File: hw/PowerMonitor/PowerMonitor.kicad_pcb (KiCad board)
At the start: 4 copper layers, 100 x 100 mm, 161 parts, among them J1 Conn_01x02_Socket, J2 Conn_01x02_Socket, J3 Conn_01x02_Socket, J4 Conn_01x02_Socket, J5 Conn_01x02_Socket, K1 Relay_SPST-NO, Q1 AO3400A, Q10 Q_PMOS_GDS, Q11 AO3400A, Q12 AO3400A, Q13 X0202MN, Q14 AO3400A, Q15 AO3400A, Q16 AO3400A, Q17 AO3400A, Q18 AO3400A, Q19 AO3400A, Q2 AO3400A, Q20 AO3400A, Q3 AO3400A, Q4 Q_PMOS_GDS, Q5 AO3400A, Q6 AO3400A, Q7 Q_PMOS_GDS, Q8 AO3400A, Q9 AO3400A, SW1 SW_Wuerth_450301014042, U1 LM393, U2 INA129, U3 LM358, U4 LM393, U5 LM358, U6 LM393, U7 LM358, U8 LM393

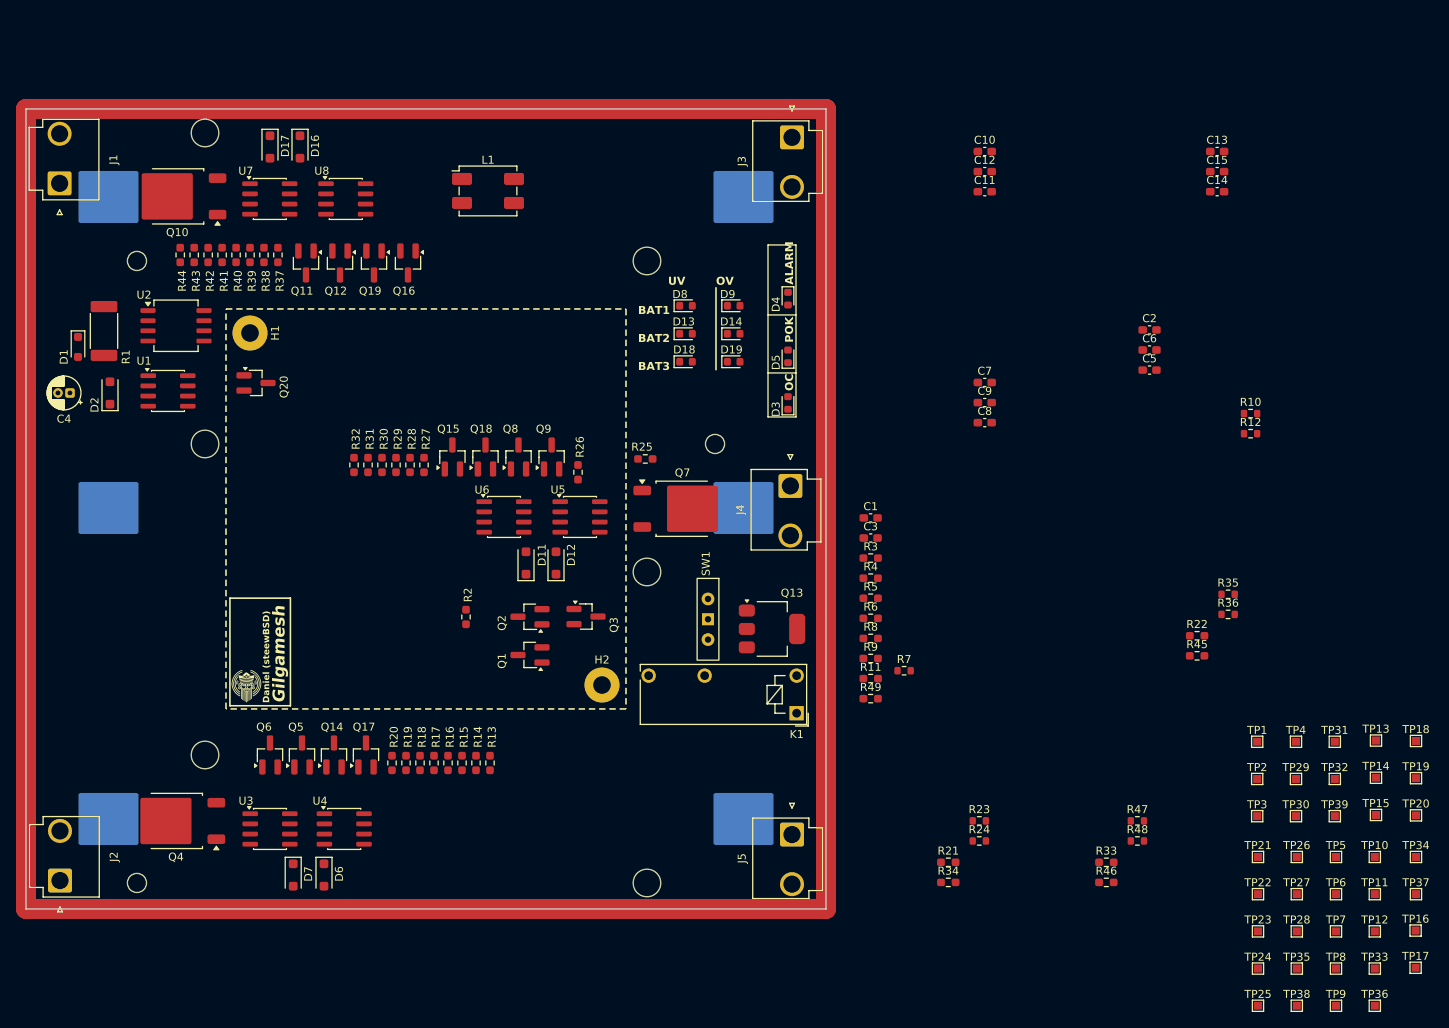
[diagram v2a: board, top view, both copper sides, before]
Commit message: finish PowerMonitor placement
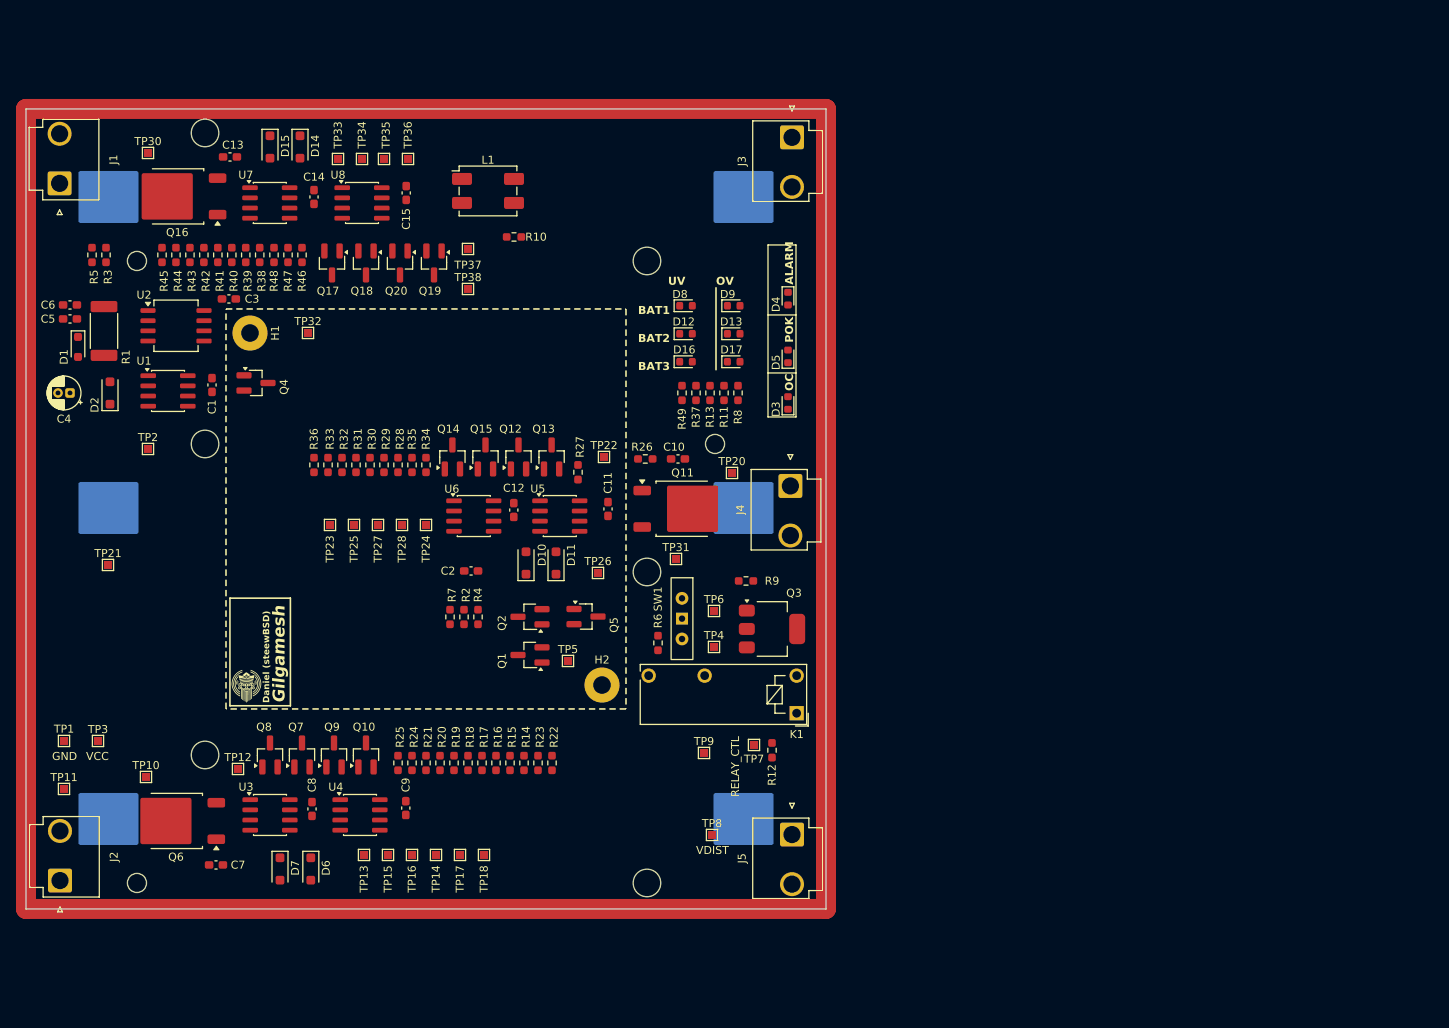
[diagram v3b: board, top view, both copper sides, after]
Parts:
- removed the R23 at (214.9, 129.5)
- removed the R35 at (246.0, 101.2)
- removed the R47 at (234.7, 129.5)
- removed the TP12 at (264.4, 143.3)
- removed the TP20 at (269.5, 128.8)
- removed the TP28 at (254.6, 143.3)
- added R24: 1K, Resistor_SMD:R_0603_1608Metric_Pad0.98x0.95mm_HandSolder, F.Cu at (144.0, 122.2)
- added R36: 1K, Resistor_SMD:R_0603_1608Metric_Pad0.98x0.95mm_HandSolder, F.Cu at (131.8, 85.0)
- added R48: 1K, Resistor_SMD:R_0603_1608Metric_Pad0.98x0.95mm_HandSolder, F.Cu at (126.8, 58.8)
- R11: renamed from R10; footprint Resistor_SMD:R_0603_1608Metric -> Resistor_SMD:R_0603_1608Metric_Pad0.98x0.95mm_HandSolder
- R13: renamed from R12; footprint Resistor_SMD:R_0603_1608Metric -> Resistor_SMD:R_0603_1608Metric_Pad0.98x0.95mm_HandSolder
- R25: renamed from R24; footprint Resistor_SMD:R_0603_1608Metric -> Resistor_SMD:R_0603_1608Metric_Pad0.98x0.95mm_HandSolder
- R37: renamed from R36; footprint Resistor_SMD:R_0603_1608Metric -> Resistor_SMD:R_0603_1608Metric_Pad0.98x0.95mm_HandSolder
- R49: renamed from R48; footprint Resistor_SMD:R_0603_1608Metric -> Resistor_SMD:R_0603_1608Metric_Pad0.98x0.95mm_HandSolder
- R8: renamed from R7; footprint Resistor_SMD:R_0603_1608Metric -> Resistor_SMD:R_0603_1608Metric_Pad0.98x0.95mm_HandSolder
- moved TP30 164.3 mm to (111.0, 46.0)
- moved TP21 160.7 mm to (106.0, 97.5)
- moved TP11 159.5 mm to (100.5, 125.5)
- moved TP3 154.7 mm to (104.8, 119.5)
- moved TP34 154.6 mm to (137.8, 46.8)
- moved TP36 153.5 mm to (143.5, 46.8)
- moved TP33 153.2 mm to (134.8, 46.8)
- moved TP35 152.1 mm to (140.5, 46.8)
- moved TP1 149.2 mm to (100.5, 119.5)
- moved TP10 149.1 mm to (110.8, 124.0)
- moved TP23 144.9 mm to (133.8, 92.5)
- moved TP2 144.7 mm to (111.0, 83.0)
- moved TP25 143.8 mm to (136.8, 92.5)
- moved TP32 140.3 mm to (131.0, 68.5)
- moved TP12 138.7 mm to (122.2, 123.0)
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- renumbered D11 to D10, D12 to D11, D13 to D12, D14 to D13, D16 to D14, D17 to D15, D18 to D16, D19 to D17, Q17 to Q10, Q7 to Q11, Q8 to Q12, Q9 to Q13, Q15 to Q14, Q18 to Q15, Q10 to Q16, Q11 to Q17, Q12 to Q18, Q16 to Q19, Q19 to Q20, Q13 to Q3, Q20 to Q4, Q3 to Q5, Q4 to Q6, Q5 to Q7, Q6 to Q8, Q14 to Q9, R9 to R10, R11 to R12, R13 to R14, R14 to R15, R15 to R16, R16 to R17, R17 to R18, R18 to R19, R19 to R20, R20 to R21, R34 to R22, R21 to R23, R25 to R26, R26 to R27, R27 to R28, R28 to R29, R29 to R30, R30 to R31, R31 to R32, R32 to R33, R45 to R34, R22 to R35, R37 to R38, R38 to R39, R39 to R40, R40 to R41, R41 to R42, R42 to R43, R43 to R44, R44 to R45, R33 to R47, R8 to R7, R49 to R9, TP5 to TP10, TP6 to TP11, TP7 to TP12, TP8 to TP13, TP33 to TP14, TP9 to TP15, TP36 to TP16, TP10 to TP17, TP11 to TP18, TP13 to TP20, TP14 to TP21, TP15 to TP22, TP16 to TP23, TP34 to TP24, TP17 to TP25, TP37 to TP26, TP18 to TP27, TP19 to TP28, TP32 to TP3, TP21 to TP30, TP22 to TP31, TP23 to TP32, TP24 to TP33, TP35 to TP34, TP25 to TP35, TP38 to TP36, TP26 to TP37, TP27 to TP38, TP29 to TP4, TP3 to TP5, TP30 to TP6, TP31 to TP7, TP39 to TP8, TP4 to TP9
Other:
- board text added: "GND"
- board text added: "RELAY_CTL"
- board text added: "VCC"
- board text added: "VDIST"

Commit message: powmon: advance routing
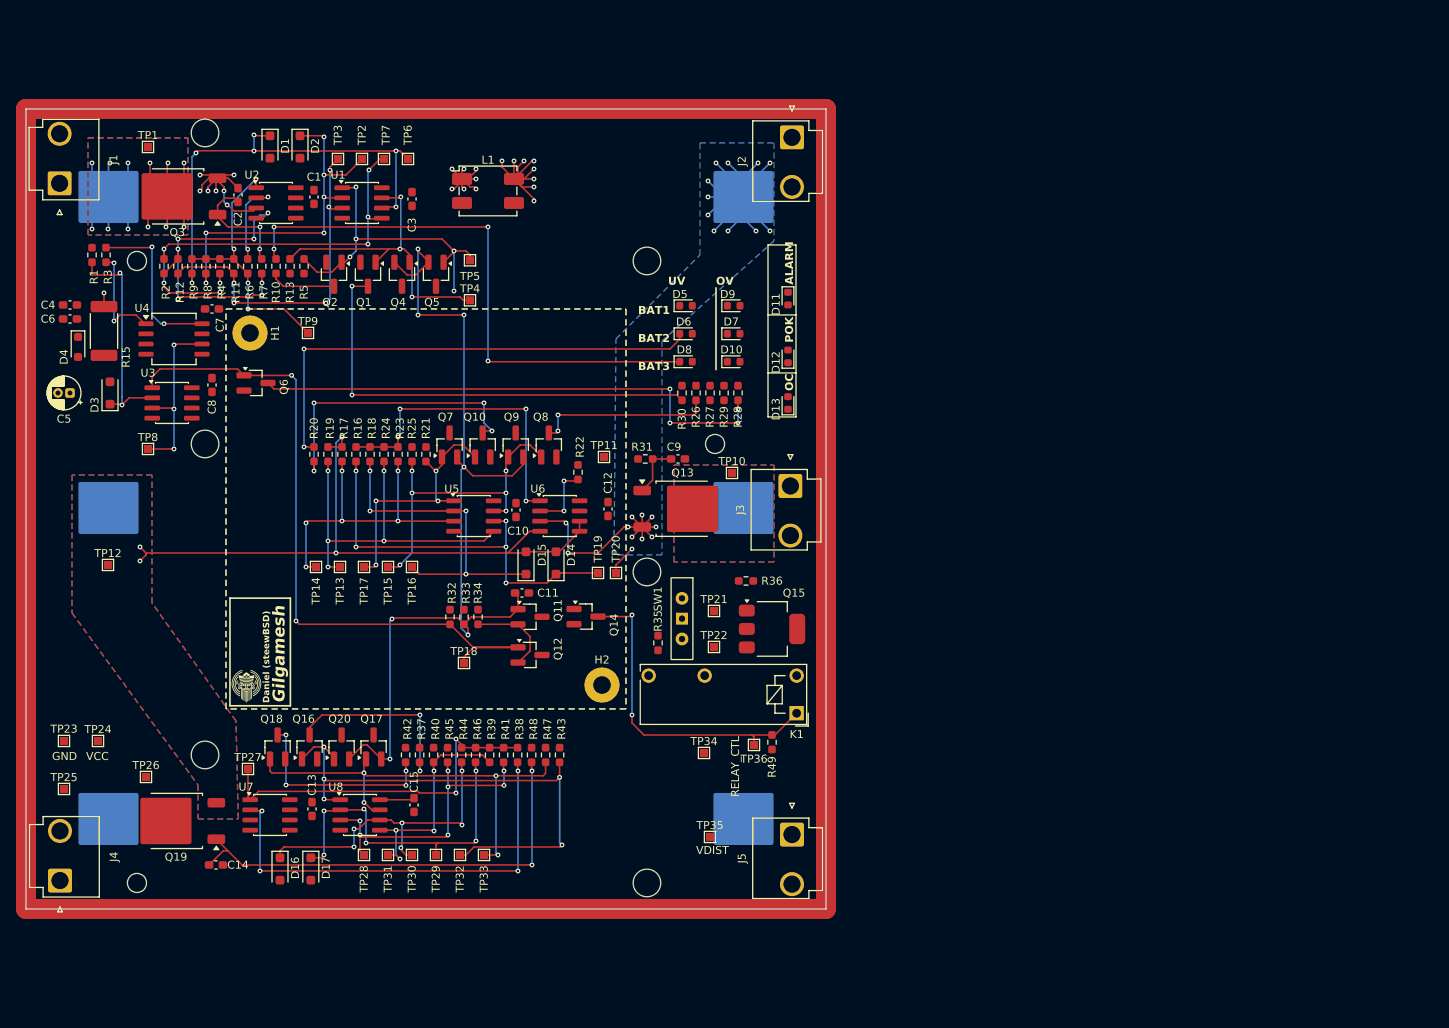
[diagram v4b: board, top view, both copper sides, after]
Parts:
- removed the R10 at (156.8, 56.5)
- moved TP18 13.0 mm to (150.5, 109.8)
- moved TP20 7.70 mm to (169.5, 98.5)
- moved C11 6.93 mm to (157.8, 101.0), turned to 180 degrees
- moved TP13 5.53 mm to (135.0, 97.8)
- moved TP14 5.53 mm to (132.0, 97.8)
- moved TP15 5.53 mm to (141.0, 97.8)
- moved TP16 5.53 mm to (144.0, 97.8)
- moved TP17 5.53 mm to (138.0, 97.8)
- moved C2 4.85 mm to (122.2, 51.2), turned to 90 degrees
- moved Q10 4.73 mm to (152.8, 82.5)
- moved Q9 4.07 mm to (157.0, 82.5)
- moved C7 2.45 mm to (119.0, 65.5), turned to 0 degrees
- moved U4 1.67 mm to (114.2, 69.2)
- moved U3 1.58 mm to (114.0, 77.2)
- moved Q7 1.54 mm to (148.7, 82.5)
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- renumbered BT1 to BT0, BT2 to BT1, BT3 to BT2, C14 to C1, C12 to C10, C2 to C11, C11 to C12, C8 to C13, C7 to C14, C9 to C15, C13 to C2, C15 to C3, C6 to C4, C4 to C5, C5 to C6, C3 to C7, C1 to C8, C10 to C9, D15 to D1, D17 to D10, D4 to D11, D5 to D12, D3 to D13, D11 to D14, D10 to D15, D7 to D16, D6 to D17, D14 to D2, D2 to D3, D1 to D4, D8 to D5, D12 to D6, D13 to D7, D16 to D8, J3 to J2, J4 to J3, J2 to J4, Q18 to Q1, Q12 to Q10, Q2 to Q11, Q1 to Q12, Q11 to Q13, Q5 to Q14, Q3 to Q15, Q7 to Q16, Q10 to Q17, Q8 to Q18, Q6 to Q19, Q17 to Q2, Q9 to Q20, Q16 to Q3, Q20 to Q4, Q19 to Q5, Q4 to Q6, Q14 to Q7, Q13 to Q8, Q15 to Q9, R5 to R1, R48 to R10, R40 to R11, R44 to R12, R47 to R13, R1 to R15, R31 to R16, R32 to R17, R30 to R18, R33 to R19, R45 to R2, R36 to R20, R34 to R21, R27 to R22, R28 to R23, R29 to R24, R35 to R25, R37 to R26, R13 to R27, R8 to R28, R11 to R29, R49 to R30, R26 to R31, R7 to R32, R2 to R33, R4 to R34, R6 to R35, R9 to R36, R24 to R37, R15 to R38, R17 to R39, R41 to R4, R21 to R40, R16 to R41, R25 to R42, R22 to R43, R19 to R44, R20 to R45, R18 to R46, R23 to R47, R14 to R48, R12 to R49, R46 to R5, R39 to R6, R38 to R7, R42 to R8, R43 to R9, TP30 to TP1, TP20 to TP10, TP22 to TP11, TP21 to TP12, TP25 to TP13, TP23 to TP14, TP28 to TP15, TP24 to TP16, TP27 to TP17, TP5 to TP18, TP26 to TP19, TP34 to TP2, TP31 to TP20, TP6 to TP21, TP4 to TP22, TP1 to TP23, TP3 to TP24, TP11 to TP25, TP10 to TP26, TP12 to TP27, TP13 to TP28, TP14 to TP29, TP33 to TP3, TP16 to TP30, TP15 to TP31, TP17 to TP32, TP18 to TP33, TP9 to TP34, TP8 to TP35, TP7 to TP36, TP38 to TP4, TP37 to TP5, TP36 to TP6, TP35 to TP7, TP2 to TP8, TP32 to TP9, U8 to U1, U7 to U2, U1 to U3, U2 to U4, U6 to U5, U5 to U6, U3 to U7, U4 to U8
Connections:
- net Net-(J1-Pin_1) renamed /VDIST
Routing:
- net /CellMonitor2/Vprot: track 0.00 -> 131.6 mm, vias 0 -> 29
- net /VOLT_ALARM: track 0.00 -> 118.1 mm, vias 0 -> 7
- net /CURR_ALARM: track 0.00 -> 87.6 mm, vias 0 -> 2
- net /CellMonitor1/Vprot: track 0.00 -> 81.9 mm, vias 0 -> 4
- net Net-(D8-K): track 0.00 -> 71.6 mm, vias 0 -> 4
- net /CellMonitor1/UNDERVOLTAGE: track 0.00 -> 67.4 mm, vias 0 -> 5
- net Net-(Q6-D): track 0.00 -> 66.1 mm, vias 0 -> 4
- net Net-(D6-K): track 0.00 -> 61.7 mm, vias 0 -> 2
- net Net-(D1-K): track 0.00 -> 57.5 mm, vias 0 -> 6
- net /CellMonitor1/OVERVOLTAGE: track 0.00 -> 57.4 mm, vias 0 -> 4
- net Net-(Q1-D): track 0.00 -> 57.1 mm, vias 0 -> 2
- net Net-(Q19-G): track 0.00 -> 56.7 mm, vias 0 -> 2
- net /CellMonitor3/VbatH: track 0.00 -> 56.3 mm, vias 0 -> 12
- net Net-(U1B-+): track 0.00 -> 55.1 mm, vias 0 -> 7
- net Net-(U7A--): track 0.00 -> 55.0 mm, vias 0 -> 4
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- added copper zone on B.Cu, net /CellMonitor1/Vprot
- added copper zone on F.Cu, net /CellMonitor1/Vprot
- added copper zone on B.Cu, net /CellMonitor2/Vprot
- added copper zone on B.Cu, net /CellMonitor3/VbatH
- added copper zone on F.Cu, net /CellMonitor3/VbatH
- added copper zone on In1.Cu, net /CellMonitor3/Vprot
- added copper zone on In1.Cu, net /VDIST
- added copper zone on B.Cu, net GND
- added copper zone on In1.Cu, net VDC

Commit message: powmon: finish routing
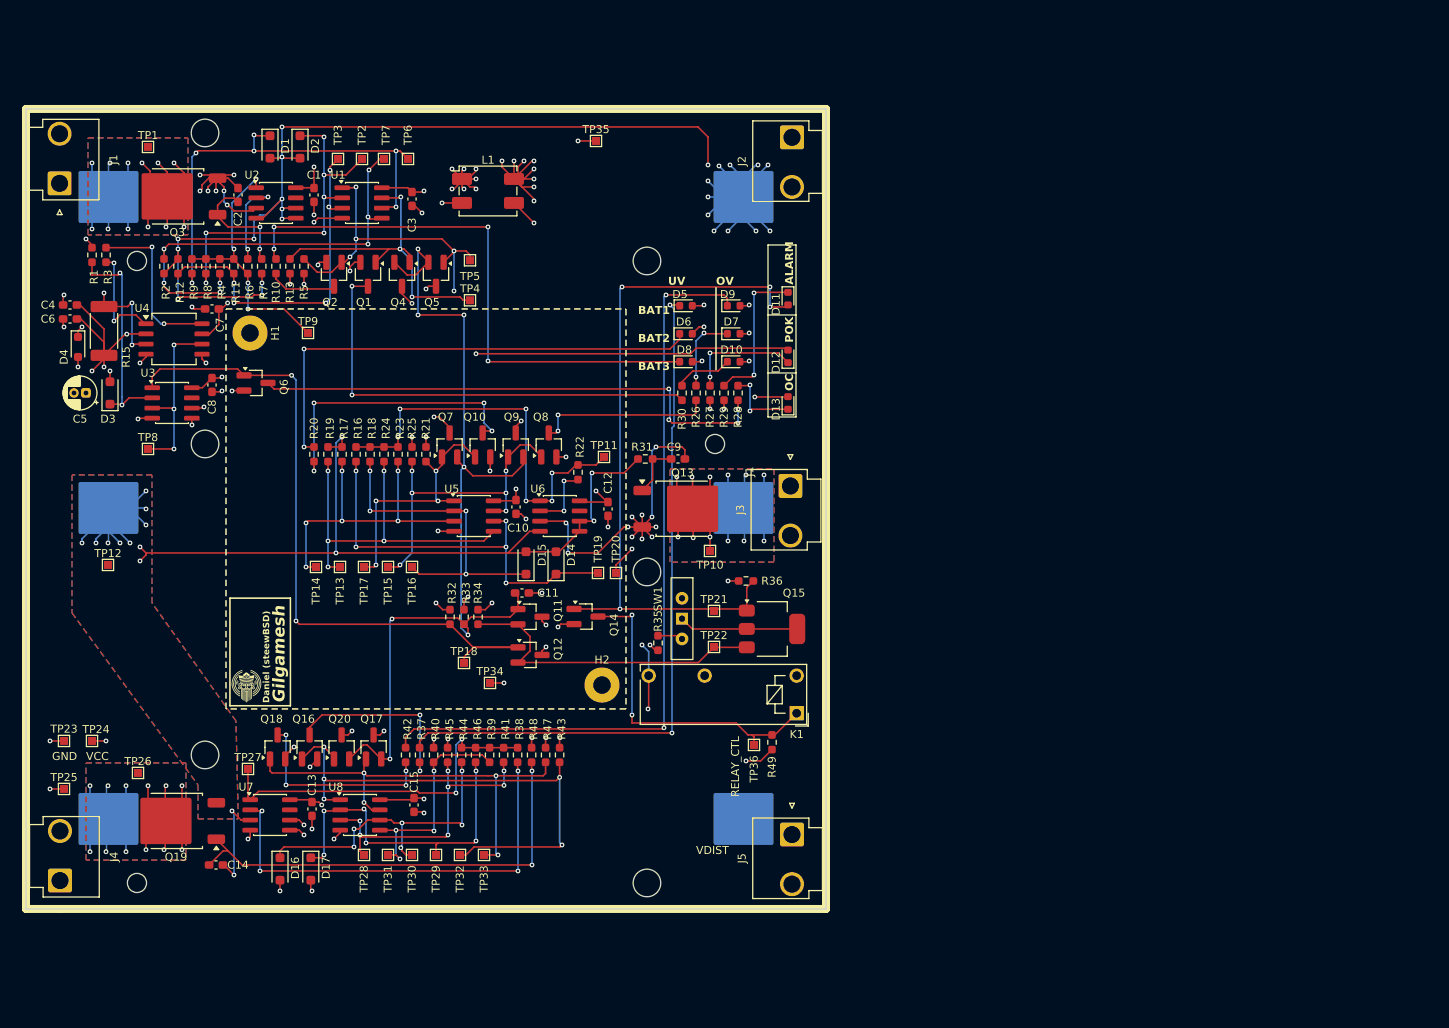
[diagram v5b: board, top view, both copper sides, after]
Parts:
- moved TP35 88.2 mm to (167.0, 44.5)
- moved TP34 28.1 mm to (153.8, 112.2)
- moved TP10 10.1 mm to (181.2, 95.8), turned to 180 degrees
- moved C5 2.00 mm to (103.2, 76.0)
- moved TP26 1.12 mm to (109.8, 123.5)
- moved TP24 0.75 mm to (104.0, 119.5)
- moved C10 0.39 mm to (157.0, 90.2)
- moved C1 0.25 mm to (131.8, 51.2)
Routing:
- net +10V: track 4.35 -> 110.2 mm, vias 0 -> 33
- net Net-(D9-K): track 0.00 -> 97.1 mm, vias 0 -> 2
- net /CellMonitor2/Vprot: track 131.6 -> 225.3 mm, vias 29 -> 35
- net Net-(D11-A): track 0.00 -> 89.4 mm, vias 0 -> 4
- net Net-(D5-K): track 0.00 -> 88.0 mm, vias 0 -> 2
- net GND: track 0.00 -> 84.9 mm, vias 0 -> 53
- net /CellMonitor1/Vprot: track 81.9 -> 148.1 mm, vias 4 -> 16
- net /CellMonitor2/VbatH: track 0.00 -> 65.8 mm, vias 0 -> 12
- net /CellMonitor1/VbatH: track 0.00 -> 56.3 mm, vias 0 -> 12
- net VDC: track 12.8 -> 54.0 mm, vias 7 -> 9
- net Net-(Q11-S): track 11.1 -> 40.5 mm
- net Net-(D11-K): track 0.00 -> 18.8 mm, vias 0 -> 2
- net Net-(SW1-B): track 0.00 -> 14.9 mm
- net Net-(D12-K): track 0.00 -> 14.3 mm, vias 0 -> 2
- net Net-(R16-Pad1): track 39.1 -> 51.4 mm, vias 4 -> 6
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- added copper zone on B.Cu, net /CellMonitor1/VbatH
- added copper zone on F.Cu, net /CellMonitor1/VbatH
- added copper zone on B.Cu, net /CellMonitor2/VbatH
- added copper zone on F.Cu, net /CellMonitor2/VbatH
- added copper zone on In1.Cu, net /CellMonitor2/Vprot
- removed copper zone on B.Cu, net /CellMonitor2/Vprot
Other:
- board text added: "J1"

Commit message: powmon: pre-fab board finishes
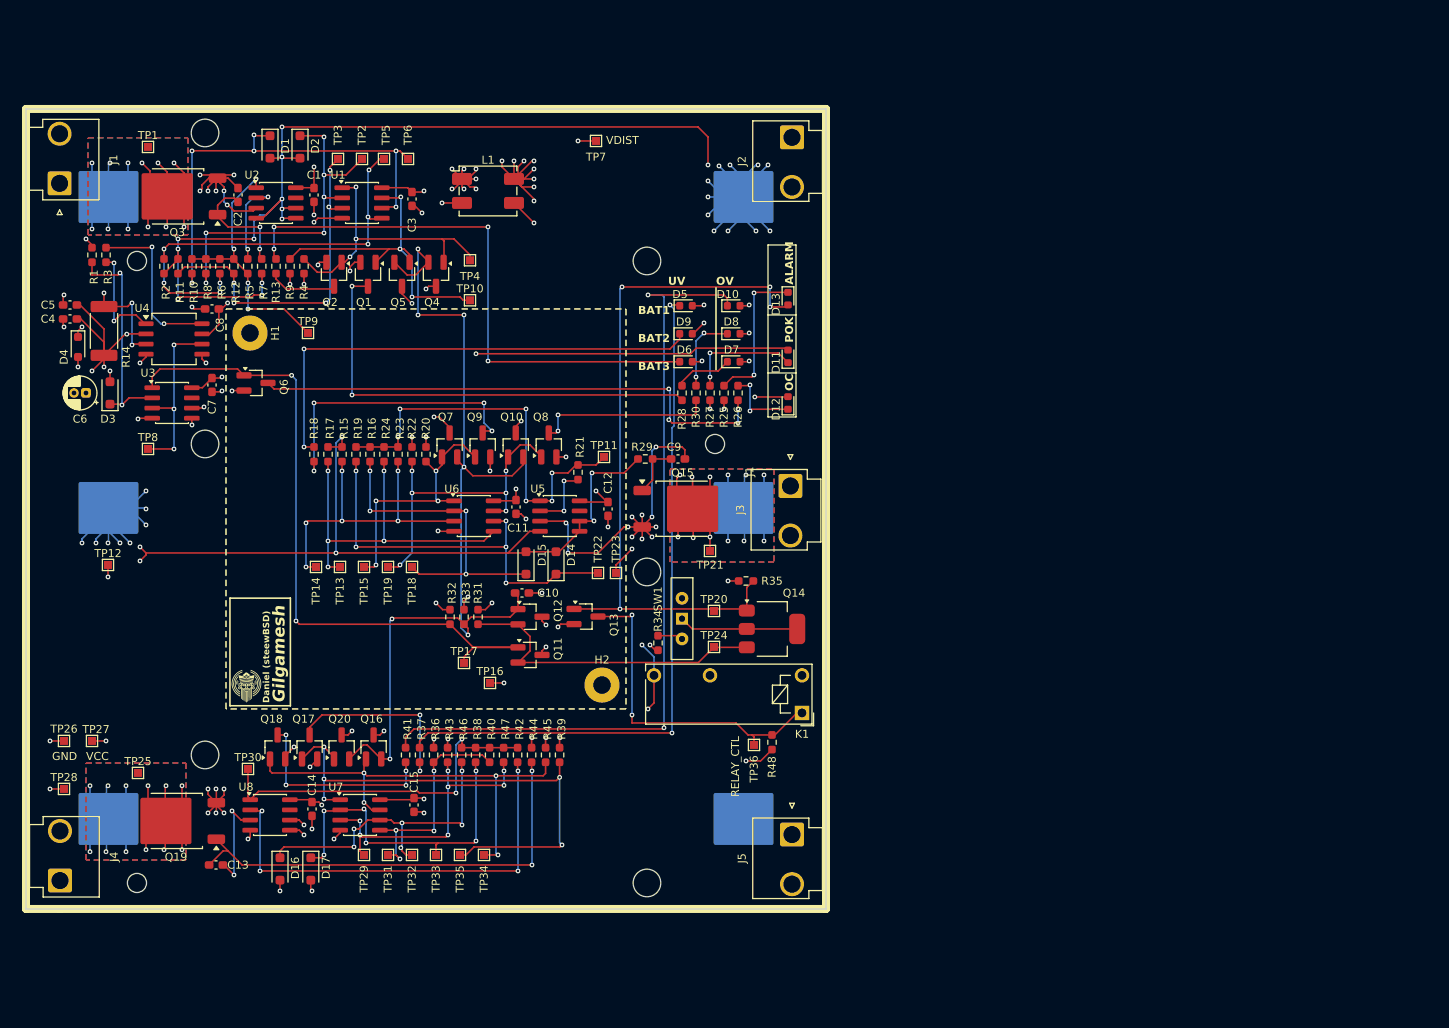
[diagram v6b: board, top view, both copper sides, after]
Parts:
- moved K1 0.67 mm to (192.8, 116.0)
- renumbered C11 to C10, C10 to C11, C14 to C13, C13 to C14, C6 to C4, C4 to C5, C5 to C6, C8 to C7, C7 to C8, D9 to D10, D12 to D11, D13 to D12, D11 to D13, D8 to D6, D10 to D7, D7 to D8, D6 to D9, Q9 to Q10, Q12 to Q11, Q11 to Q12, Q14 to Q13, Q15 to Q14, Q13 to Q15, Q17 to Q16, Q16 to Q17, Q5 to Q4, Q4 to Q5, Q10 to Q9, R9 to R10, R12 to R11, R11 to R12, R10 to R13, R15 to R14, R17 to R15, R18 to R16, R19 to R17, R20 to R18, R16 to R19, R21 to R20, R22 to R21, R25 to R22, R29 to R25, R28 to R26, R30 to R28, R31 to R29, R26 to R30, R34 to R31, R35 to R34, R36 to R35, R40 to R36, R46 to R38, R43 to R39, R5 to R4, R39 to R40, R42 to R41, R38 to R42, R45 to R43, R48 to R44, R47 to R45, R44 to R46, R41 to R47, R49 to R48, R6 to R5, R4 to R6, R13 to R9, TP4 to TP10, TP17 to TP15, TP34 to TP16, TP18 to TP17, TP16 to TP18, TP15 to TP19, TP21 to TP20, TP10 to TP21, TP19 to TP22, TP20 to TP23, TP22 to TP24, TP26 to TP25, TP23 to TP26, TP24 to TP27, TP25 to TP28, TP28 to TP29, TP27 to TP30, TP30 to TP32, TP29 to TP33, TP33 to TP34, TP32 to TP35, TP5 to TP4, TP7 to TP5, TP35 to TP7, U6 to U5, U5 to U6, U8 to U7, U7 to U8
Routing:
- net /CellMonitor1/Vprot: track 148.1 -> 160.3 mm, vias 16 -> 23
- net Net-(D10-K): track 97.1 -> 101.1 mm
- net /CellMonitor3/UNDERVOLTAGE: track 40.7 -> 36.8 mm, vias 5 -> 3
- net /CellMonitor2/VbatH: track 65.8 -> 62.8 mm
- net +10V: track 110.2 -> 111.8 mm
- net Net-(U1A-+): track 44.1 -> 43.4 mm
- net Net-(Q13-D): track 41.5 -> 42.2 mm
- added copper zone on In1.Cu, net /CellMonitor1/Vprot
- removed copper zone on B.Cu, net /CellMonitor1/Vprot
- removed copper zone on F.Cu, net /CellMonitor1/Vprot
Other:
- board text added: "0.2000 mm / 0.1000 mm"
- board text added: "0.3000 mm"
- board text added: "1.6000 mm"
- board text added: "100.0000 mm x 100.0000 mm"
- board text added: "4"
- board text added: "BOARD CHARACTERISTICS"
- board text added: "Board Thickness:"
- board text added: "Board overall dimensions:"
- board text added: "Castellated pads:"
- board text added: "Copper Finish:"
- board text added: "Copper Layer Count:"
- board text added: "Edge card connectors:"
- board text added: "HAL SnPb"
- board text added: "Impedance Control:"
- board text added: "Min hole diameter:"
- board text added: "Min track/spacing:"
- board text added: "No"
- board text added: "Plated Board Edge:"
